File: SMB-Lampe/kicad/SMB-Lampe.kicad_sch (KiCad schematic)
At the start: 2 parts, among them P1 USB_C_Plug_USB2.0, SW1 SW_SPST

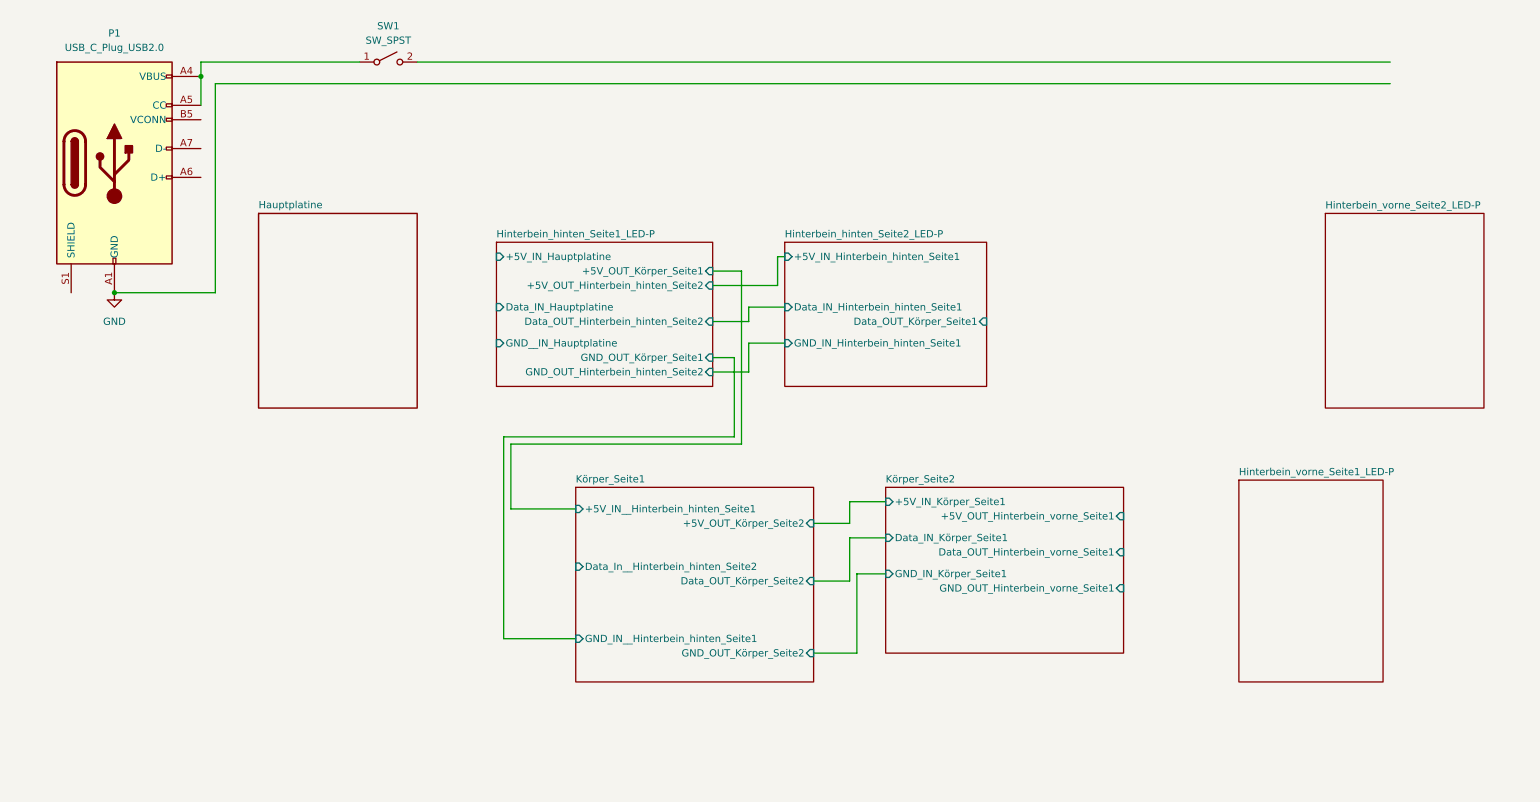
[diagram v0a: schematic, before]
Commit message: Vorderes Hinterbein fertig
Alle Platinen sind fertig beschaltet
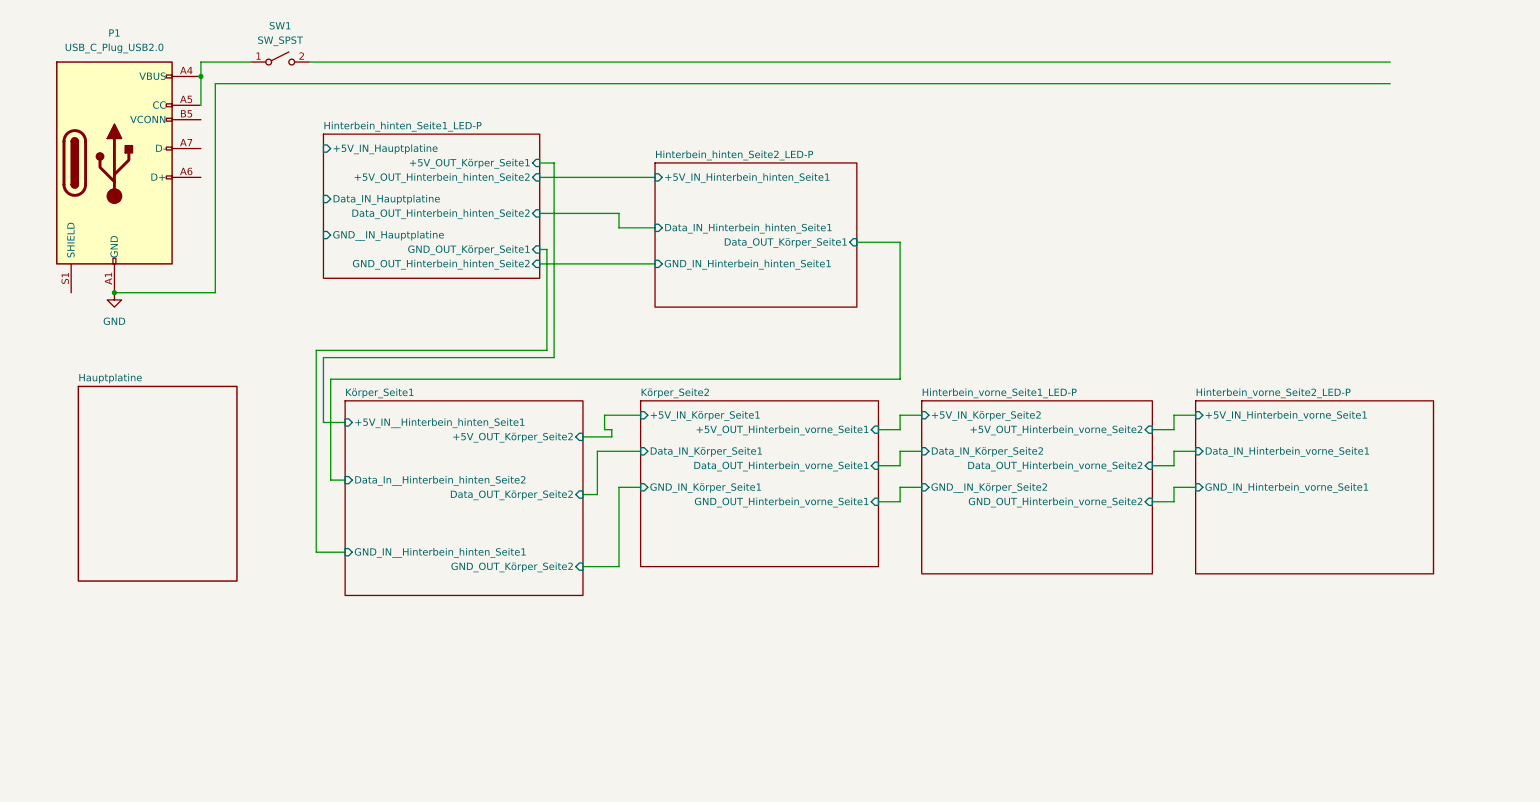
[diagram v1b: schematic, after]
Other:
- sheet Hinterbein_vorne_Seite1_LED-P ports: added +5V_IN_Körper_Seite2, +5V_OUT_Hinterbein_vorne_Seite2, Data_IN_Körper_Seite2, Data_OUT_Hinterbein_vorne_Seite2, GND_OUT_Hinterbein_vorne_Seite2, GND__IN_Körper_Seite2; removed none
- sheet Hinterbein_vorne_Seite2_LED-P ports: added +5V_IN_Hinterbein_vorne_Seite1, Data_IN_Hinterbein_vorne_Seite1, GND_IN_Hinterbein_vorne_Seite1; removed none
- moved on the sheet: SW1

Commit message: Hauptplatine fertig
Hauptplatine mit ESP Levelshifter und Screwsockets
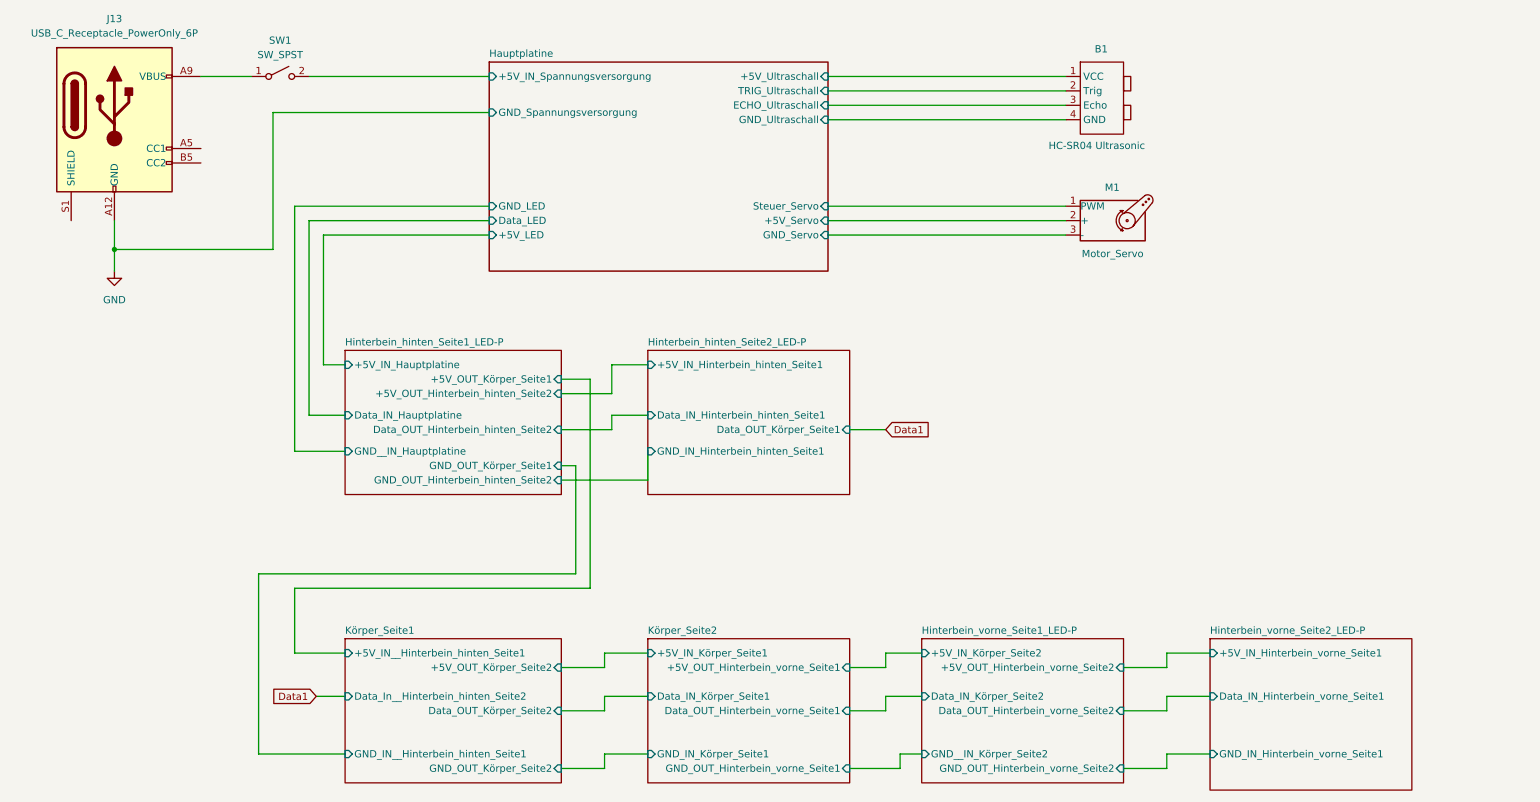
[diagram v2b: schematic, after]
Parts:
- removed P1: USB_C_Plug_USB2.0, symbol Connector:USB_C_Plug_USB2.0
- added B1: HC-SR04 Ultrasonic, symbol Eigene _Library:HC-SR04
- added J13: USB_C_Receptacle_PowerOnly_6P, symbol Connector:USB_C_Receptacle_PowerOnly_6P
- added M1: Motor_Servo, symbol Motor:Motor_Servo
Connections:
- net GND: now also J13.A12 (GND), J13.B12 (GND)
- net at SW1.1 (A): now also J13.A9 (VBUS), J13.B9 (VBUS)
- net Hauptplatine/+5V_IN_Spannungsversorgung: now reaches SW1.2 (B)
- new net Hauptplatine/+5V_Servo: M1.2 (+)
- new net Hauptplatine/+5V_Ultraschall: B1.1 (VCC)
- new net Hauptplatine/ECHO_Ultraschall: B1.3 (Echo)
- new net Hauptplatine/GND_Servo: M1.3 (-)
- new net Hauptplatine/GND_Ultraschall: B1.4 (GND)
- new net Hauptplatine/Steuer_Servo: M1.1 (PWM)
- new net Hauptplatine/TRIG_Ultraschall: B1.2 (Trig)
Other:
- sheet Hauptplatine ports: added +5V_IN_Spannungsversorgung, +5V_LED, +5V_Servo, +5V_Ultraschall, Data_LED, ECHO_Ultraschall, GND_LED, GND_Servo, GND_Spannungsversorgung, GND_Ultraschall, Steuer_Servo, TRIG_Ultraschall; removed none
- moved on the sheet: SW1

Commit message: Nachträgliche Änderungen für die Fertigung und Präsentation
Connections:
- net Hauptplatine/+5V_Servo is gone; now on net rd: M1.2 (+)
- net Hauptplatine/+5V_Ultraschall is gone; now on net rd: B1.1 (VCC)
- net Hauptplatine/GND_Ultraschall is gone; now on net GND: B1.4 (GND)
- net Hauptplatine/+5V_IN_Spannungsversorgung renamed rd
- net Hauptplatine/ECHO_Ultraschall renamed wh
- net Hauptplatine/GND_Servo renamed bn
- net Hauptplatine/Steuer_Servo renamed ye
- net Hauptplatine/TRIG_Ultraschall renamed vt

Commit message: vor Schaltplananpassung
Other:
- company: (none) -> IFM / Lukas Gulde
- title: (none) -> Projektaarbeit SMB-Lampe
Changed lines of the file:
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@@
 	(generator_version "9.0")
 	(paper "A4")
+	(title_block
+		(title "Projektaarbeit SMB-Lampe")
+		(date "2026-03-31")
+		(company "IFM / Lukas Gulde")
+		(comment 1 "Gesamtschaltplan")
+	)
 	(junction
 		(at 35.56 58.42)
@@
 		)
 	)
-	(label "bu"
+	(label ""
+		(at 125.73 129.54 0)
+		(effects
+			(font
+				(size 1.27 1.27)
+			)
+			(justify left bottom)
+		)
+	)
+	(label "bk"
 		(at 116.84 96.52 0)
 		(effects
@@
 		)
 	)
-	(label "bu"
+	(label "bk"
 		(at 96.52 50.8 0)
 		(effects
@@
 		)
 	)
-	(label "bu"
+	(label "bk"
 		(at 168.91 149.86 0)
 		(effects
